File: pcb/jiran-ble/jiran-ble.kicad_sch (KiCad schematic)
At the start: 167 parts, among them J1 BATT, J2 USB-C Connector, J3 SWD, J4 BATT, J5 USB-C Connector, J6 SWD, Q1 SI2301CDS-T1-GE3, Q2 SI2301CDS-T1-GE3, SW1 SW_DPDT_x2, SW10 SW_Push, SW11 SW_Push, SW12 SW_Push, SW13 SW_Push, SW14 SW_Push, SW15 SW_Push, SW16 SW_Push, SW17 SW_Push, SW18 SW_Push, SW19 SW_Push, SW2 SW_Push, SW20 SW_Push, SW21 SW_Push, SW22 SW_Push, SW23 SW_Push, SW24 SW_Push, SW25 SW_Push, SW26 SW_Push, SW27 SW_Push, SW28 SW_Push, SW29 SW_Push, SW3 SW_Push, SW30 SW_Push, SW31 SW_Push, SW32 SW_Push, SW33 SW_Push, SW34 SW_Push, SW35 SW_Push, SW36 SW_Push, SW37 SW_Push, SW38 SW_Push, SW39 SW_Push, SW4 SW_Push, SW40 SW_Push, SW41 SW_Push, SW42 SW_Push, SW43 SW_Push, SW44 SW_Push, SW45 SW_Push, SW46 SW_Push, SW47 SW_Push, SW48 SW_Push, SW49 SW_Push, SW5 SW_Push, SW50 SW_Push, SW51 SW_Push, SW52 SW_Push, SW53 SW_Push, SW54 SW_Push, SW55 SW_Push, SW56 SW_Push, SW57 SW_Push, SW58 SW_Push, SW59 SW_Push, SW6 SW_Push, SW7 SW_Push, SW8 SW_Push, SW9 SW_Push, U1 HOLYIOT-18010-NRF52840_simple, U2 XC6220B331MR-G, U3 TP4054, U4 HOLYIOT-18010-NRF52840_simple, U5 XC6220B331MR-G, U6 TP4054

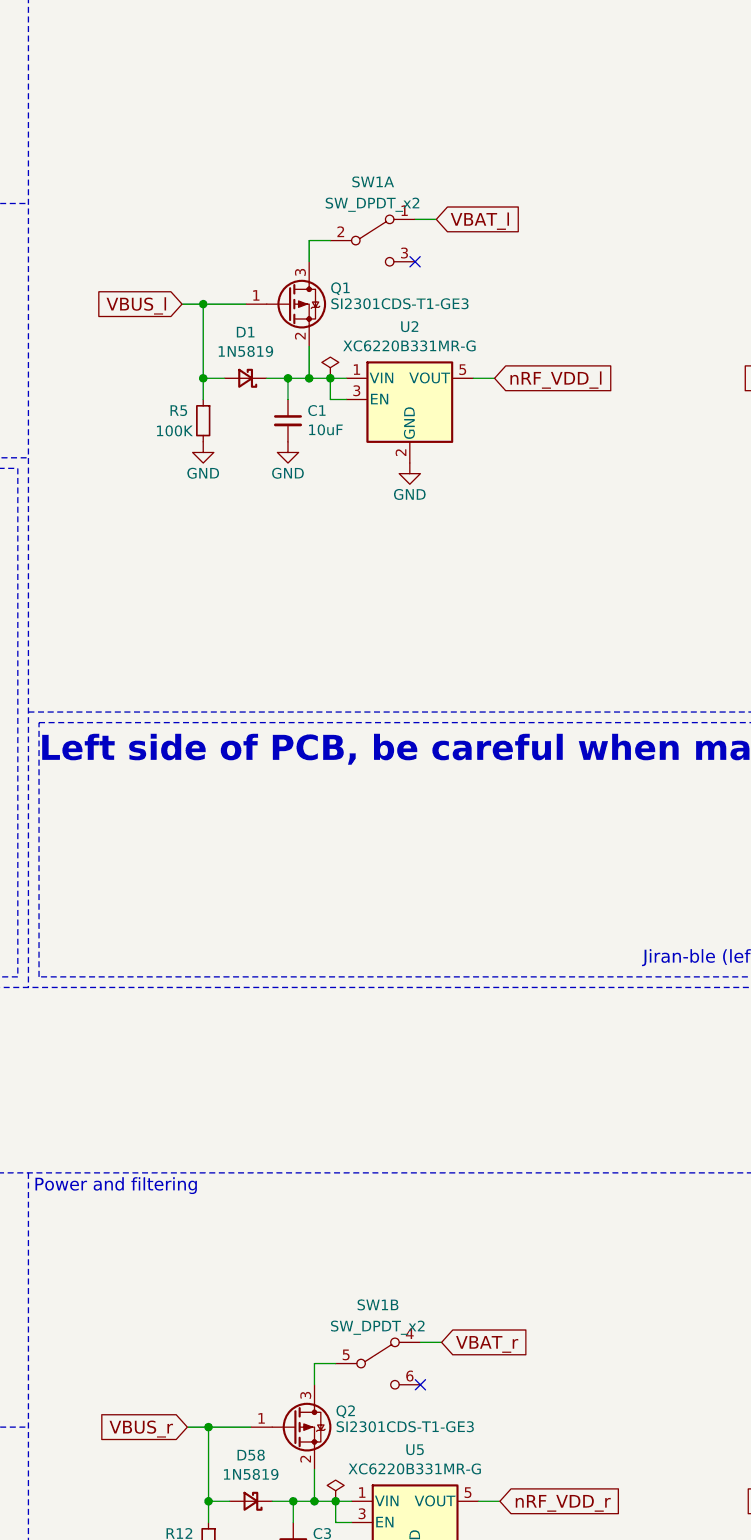
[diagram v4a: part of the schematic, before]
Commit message: Mirror toggle swithc
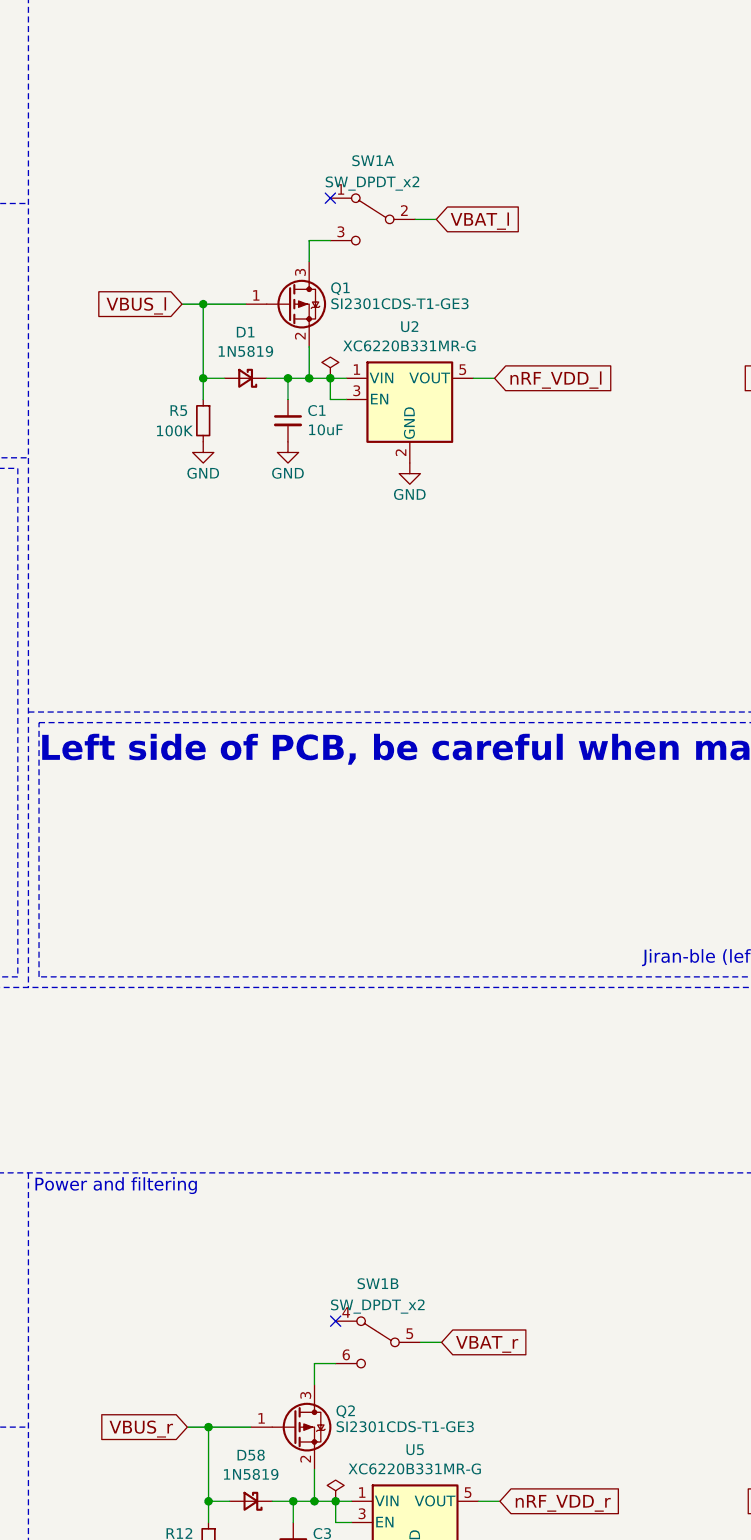
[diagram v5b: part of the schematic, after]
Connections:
- net VBAT_l: now also SW1.2 (B); no longer SW1.1 (A)
- net VBAT_r: now also SW1.5 (B); no longer SW1.4 (A)
- net at Q1.3 (D): now also SW1.3 (C); no longer SW1.2 (B)
- net at Q2.3 (D): now also SW1.6 (C); no longer SW1.5 (B)
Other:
- moved on the sheet: SW1A, SW1B
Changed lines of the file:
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@@
   (no_connect (at 133.35 201.295))
   (no_connect (at 133.35 203.835))
-  (no_connect (at 330.835 50.165))
-  (no_connect (at 331.47 184.785))
+  (no_connect (at 320.675 42.545))
+  (no_connect (at 321.31 177.165))
   (wire (pts (xy 25.4 106.68) (xy 25.4 123.825))
     (stroke (width 0) (type solid) (color 0 0 0 0))
@@
     (pin "2")
   )
-  (symbol (lib_id "Switch:SW_DPDT_x2") (at 325.755 47.625 0) (unit 1)
+  (symbol (lib_id "Switch:SW_DPDT_x2") (at 325.755 45.085 0) (mirror y) (unit 1)
     (in_bom yes) (on_board yes)
-    (property "Reference" "SW1" (id 0) (at 325.755 40.64 0))
-    (property "Value" "SW_DPDT_x2" (id 1) (at 325.755 43.18 0))
-    (property "Footprint" "jiran-ble:Switch_SMD_MSK-12C02" (id 2) (at 325.755 47.625 0)
+    (property "Reference" "SW1" (id 0) (at 325.755 38.1 0))
+    (property "Value" "SW_DPDT_x2" (id 1) (at 325.755 40.64 0))
+    (property "Footprint" "jiran-ble:Switch_SMD_MSK-12C02" (id 2) (at 325.755 45.085 0)
       (effects (font (size 1.27 1.27)) hide)
     )
-    (property "Datasheet" "~" (id 3) (at 325.755 47.625 0)
+    (property "Datasheet" "~" (id 3) (at 325.755 45.085 0)
       (effects (font (size 1.27 1.27)) hide)
     )
@@
     (pin "3")
   )
-  (symbol (lib_id "Switch:SW_DPDT_x2") (at 326.39 182.245 0) (unit 2)
+  (symbol (lib_id "Switch:SW_DPDT_x2") (at 326.39 179.705 0) (mirror y) (unit 2)
     (in_bom yes) (on_board yes)
-    (property "Reference" "SW1" (id 0) (at 326.39 175.26 0))
-    (property "Value" "SW_DPDT_x2" (id 1) (at 326.39 177.8 0))
-    (property "Footprint" "jiran-ble:Switch_SMD_MSK-12C02" (id 2) (at 326.39 182.245 0)
+    (property "Reference" "SW1" (id 0) (at 326.39 172.72 0))
+    (property "Value" "SW_DPDT_x2" (id 1) (at 326.39 175.26 0))
+    (property "Footprint" "jiran-ble:Switch_SMD_MSK-12C02" (id 2) (at 326.39 179.705 0)
       (effects (font (size 1.27 1.27)) hide)
     )
-    (property "Datasheet" "~" (id 3) (at 326.39 182.245 0)
+    (property "Datasheet" "~" (id 3) (at 326.39 179.705 0)
       (effects (font (size 1.27 1.27)) hide)
     )

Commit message: Edit contains
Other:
- note added: "Left side contain: SW1 - SW29 D1 - D29 R1 - R9 HM1 - HM5 U1 - U3 J1 - J3 LED1 - LED2 C1 - C2 SW1A G1"
- note added: "Right side contain: SW30 - SW59 D30 - D58 R10 - R18 HM6 - HM10 U4 - U6 J4 - J6 LED3 - LED4 C3 - C4 SW1B G2"
- note removed: "Left side contain: SW1 - SW30 D1 - D29 R1 - R9 HM1 - HM5 U1 - U3 J1 - J4 LED1 - LED2 C1 - C2 SW2A G1"
- note removed: "Right side contain: SW31 - SW59 D30 - D58 R10 - R18 HM6 - HM10 U4 - U6 J5 - J8 LED3 - LED4 C3 - C4 SW2B G2"
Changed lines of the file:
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@@
     (effects (font (size 1.524 1.524)) (justify left bottom))
   )
-  (text "Left side contain:\nSW1 - SW30\nD1 - D29\nR1 - R9\nHM1 - HM5\nU1 - U3\nJ1 - J4\nLED1 - LED2\nC1 - C2\nSW2A\nG1\n"
+  (text "Left side contain:\nSW1 - SW29\nD1 - D29\nR1 - R9\nHM1 - HM5\nU1 - U3\nJ1 - J3\nLED1 - LED2\nC1 - C2\nSW1A\nG1\n"
     (at 247.015 102.87 0)
     (effects (font (size 1.5494 1.5494)) (justify left bottom))
   )
-  (text "Right side contain:\nSW31 - SW59\nD30 - D58\nR10 - R18\nHM6 - HM10\nU4 - U6\nJ5 - J8\nLED3 - LED4\nC3 - C4\nSW2B\nG2\n"
+  (text "Right side contain:\nSW30 - SW59\nD30 - D58\nR10 - R18\nHM6 - HM10\nU4 - U6\nJ4 - J6\nLED3 - LED4\nC3 - C4\nSW1B\nG2\n"
     (at 247.015 250.19 0)
     (effects (font (size 1.5494 1.5494)) (justify left bottom))

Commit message: Backups, cache update, etc.
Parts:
- J1, J4: footprint jiran-ble:Connector_THT_1x2_2.54 -> jiran-ble:JST_ZH_1x2_P1.5
- SW58, SW59: footprint (none) -> jiran-ble:TS-1086E
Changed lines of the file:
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@@
       (effects (font (size 1.27 1.27)) (justify left))
     )
-    (property "Footprint" "jiran-ble:Connector_THT_1x2_2.54" (id 2) (at 258.445 26.035 0)
+    (property "Footprint" "jiran-ble:JST_ZH_1x2_P1.5" (id 2) (at 258.445 26.035 0)
       (effects (font (size 1.27 1.27)) hide)
     )
@@
       (effects (font (size 1.27 1.27)) (justify left))
     )
-    (property "Footprint" "jiran-ble:Connector_THT_1x2_2.54" (id 2) (at 258.445 172.72 0)
+    (property "Footprint" "jiran-ble:JST_ZH_1x2_P1.5" (id 2) (at 258.445 172.72 0)
       (effects (font (size 1.27 1.27)) hide)
     )
@@
     (property "Reference" "SW58" (id 0) (at 194.31 22.225 0))
     (property "Value" "SW_Push" (id 1) (at 194.31 24.765 0))
-    (property "Footprint" "" (id 2) (at 194.31 23.495 0)
+    (property "Footprint" "jiran-ble:TS-1086E" (id 2) (at 194.31 23.495 0)
       (effects (font (size 1.27 1.27)) hide)
     )
@@
     (property "Reference" "SW59" (id 0) (at 194.31 168.91 0))
     (property "Value" "SW_Push" (id 1) (at 194.31 171.45 0))
-    (property "Footprint" "" (id 2) (at 194.31 170.18 0)
+    (property "Footprint" "jiran-ble:TS-1086E" (id 2) (at 194.31 170.18 0)
       (effects (font (size 1.27 1.27)) hide)
     )
@@
     )
     (path "/00000000-0000-0000-0000-0000602e539e"
-      (reference "J1") (unit 1) (value "BATT") (footprint "jiran-ble:Connector_THT_1x2_2.54")
+      (reference "J1") (unit 1) (value "BATT") (footprint "jiran-ble:JST_ZH_1x2_P1.5")
     )
     (path "/00000000-0000-0000-0000-00005c743564"
@@
     )
     (path "/00000000-0000-0000-0000-00006130bcb8"
-      (reference "J4") (unit 1) (value "BATT") (footprint "jiran-ble:Connector_THT_1x2_2.54")
+      (reference "J4") (unit 1) (value "BATT") (footprint "jiran-ble:JST_ZH_1x2_P1.5")
     )
     (path "/00000000-0000-0000-0000-00006130bccf"
@@
     )
     (path "/dc86d0da-0f20-467e-a7e3-62aa396e175e"
-      (reference "SW58") (unit 1) (value "SW_Push") (footprint "")
+      (reference "SW58") (unit 1) (value "SW_Push") (footprint "jiran-ble:TS-1086E")
     )
     (path "/d4ebf227-7643-4474-8ab3-9d19d7f50330"
-      (reference "SW59") (unit 1) (value "SW_Push") (footprint "")
+      (reference "SW59") (unit 1) (value "SW_Push") (footprint "jiran-ble:TS-1086E")
     )
     (path "/00000000-0000-0000-0000-00006068c8f8"

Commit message: Backups update, assign footprints
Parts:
- J2, J5: footprint jiran-ble:USB-C-31-M-12 -> jiran-ble:USB-C-31-M-27
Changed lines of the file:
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@@
     (property "Reference" "J2" (id 0) (at 118.11 20.955 0))
     (property "Value" "USB-C Connector" (id 1) (at 118.11 22.86 0))
-    (property "Footprint" "jiran-ble:USB-C-31-M-12" (id 2) (at 120.8278 22.225 0)
+    (property "Footprint" "jiran-ble:USB-C-31-M-27" (id 2) (at 120.8278 22.225 0)
       (effects (font (size 1.27 1.27)) hide)
     )
@@
     (property "Reference" "J5" (id 0) (at 118.11 167.64 0))
     (property "Value" "USB-C Connector" (id 1) (at 118.11 169.545 0))
-    (property "Footprint" "jiran-ble:USB-C-31-M-12" (id 2) (at 120.8278 168.91 0)
+    (property "Footprint" "jiran-ble:USB-C-31-M-27" (id 2) (at 120.8278 168.91 0)
       (effects (font (size 1.27 1.27)) hide)
     )
@@
     )
     (path "/00000000-0000-0000-0000-00005c743564"
-      (reference "J2") (unit 1) (value "USB-C Connector") (footprint "jiran-ble:USB-C-31-M-12")
+      (reference "J2") (unit 1) (value "USB-C Connector") (footprint "jiran-ble:USB-C-31-M-27")
     )
     (path "/00000000-0000-0000-0000-00005e8fc792"
@@
     )
     (path "/00000000-0000-0000-0000-00006130bccf"
-      (reference "J5") (unit 1) (value "USB-C Connector") (footprint "jiran-ble:USB-C-31-M-12")
+      (reference "J5") (unit 1) (value "USB-C Connector") (footprint "jiran-ble:USB-C-31-M-27")
     )
     (path "/00000000-0000-0000-0000-00006130bc59"
